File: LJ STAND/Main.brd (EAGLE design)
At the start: 180 x 152 mm, 211 parts, among them Q1 200mA/50V

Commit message: Some small fixes to the main pcb
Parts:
- R15, R24, R33, R42: value 1.5K -> 1K
- moved LOGIC_SWITCH 2.24 mm to (37.1, 56.0)
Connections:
- net LIGHT_GATE_LASER: now also MASTER.21, MASTER.22, MASTER.23
- net LIGHT_GATE_OUT: now also MASTER.20
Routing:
- net LIGHT_GATE_OUT: track 0.00 -> 38.7 mm
- net LIGHT_GATE_LASER: track 0.00 -> 37.1 mm
- net N$12: track 42.9 -> 45.4 mm
- net N$2: track 12.7 -> 15.0 mm
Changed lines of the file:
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@@
 <attribute name="VALUE" x="107.40568125" y="56.8268" size="0.4064" layer="28" font="vector" rot="MR180"/>
 </element>
-<element name="R15" library="SparkFun-Resistors" package="0603-RES" value="1.5K" x="105.4706" y="49.6222" smashed="yes" rot="MR270">
+<element name="R15" library="SparkFun-Resistors" package="0603-RES" value="1K" x="105.4706" y="49.6222" smashed="yes" rot="MR270">
 <attribute name="VALUE" x="104.8606" y="47.86848125" size="0.4064" layer="28" font="vector" rot="MR180"/>
 </element>
@@
 <attribute name="VALUE" x="85.58931875" y="53.3058375" size="0.4064" layer="28" font="vector" rot="MR180"/>
 </element>
-<element name="R24" library="SparkFun-Resistors" package="0603-RES" value="1.5K" x="82.9956" y="54.4308" smashed="yes" rot="MR0">
+<element name="R24" library="SparkFun-Resistors" package="0603-RES" value="1K" x="82.9956" y="54.4308" smashed="yes" rot="MR0">
 <attribute name="VALUE" x="83.595040625" y="53.0744375" size="0.4064" layer="28" font="vector" rot="MR0"/>
 </element>
@@
 <attribute name="VALUE" x="109.9334" y="26.1756" size="0.4064" layer="28" font="vector" rot="MR270"/>
 </element>
-<element name="R33" library="SparkFun-Resistors" package="0603-RES" value="1.5K" x="106.9616" y="23.2394" smashed="yes" rot="MR270">
+<element name="R33" library="SparkFun-Resistors" package="0603-RES" value="1K" x="106.9616" y="23.2394" smashed="yes" rot="MR270">
 <attribute name="VALUE" x="106.239640625" y="21.3788375" size="0.4064" layer="28" font="vector" rot="MR180"/>
 </element>
@@
 <attribute name="VALUE" x="108.42411875" y="41.948278125" size="0.4064" layer="28" font="vector" rot="MR180"/>
 </element>
-<element name="R42" library="SparkFun-Resistors" package="0603-RES" value="1.5K" x="106.3322" y="37.9866" smashed="yes" rot="MR270">
+<element name="R42" library="SparkFun-Resistors" package="0603-RES" value="1K" x="106.3322" y="37.9866" smashed="yes" rot="MR270">
 <attribute name="VALUE" x="105.696121875" y="36.131678125" size="0.4064" layer="28" font="vector" rot="MR180"/>
 </element>
@@
 </element>
 <element name="MOTOR_SWITCH" library="jst-vh" package="B2P-VH" value="" x="39.3702" y="44.6026" smashed="yes" rot="R270">
-<attribute name="NAME" x="44.5546" y="39.3656" size="1.016" layer="25" font="vector" ratio="10" rot="R180"/>
+<attribute name="NAME" x="44.676521875" y="38.5629625" size="1.016" layer="25" font="vector" ratio="10" rot="R180"/>
 <attribute name="VALUE" x="32.3702" y="47.6026" size="1.27" layer="27" rot="R270"/>
 </element>
-<element name="LOGIC_SWITCH" library="jst-vh" package="B2P-VH" value="" x="39.3442" y="56.058" smashed="yes" rot="R270">
-<attribute name="NAME" x="43.945" y="51.0756" size="1.016" layer="25" font="vector" ratio="10" rot="R180"/>
-<attribute name="VALUE" x="32.3442" y="59.058" size="1.27" layer="27" rot="R270"/>
+<element name="LOGIC_SWITCH" library="jst-vh" package="B2P-VH" value="" x="37.109" y="56.0072" smashed="yes" rot="R270">
+<attribute name="NAME" x="41.78091875" y="50.831759375" size="1.016" layer="25" font="vector" ratio="10" rot="R180"/>
+<attribute name="VALUE" x="30.109" y="59.0072" size="1.27" layer="27" rot="R270"/>
 </element>
 <element name="C14" library="SparkFun-Capacitors" package="0805" value="0.1uF" x="42.1638" y="129.4132" smashed="yes" rot="R180">
@@
 <via x="25.3746" y="65.4304" extent="1-16" drill="0.508"/>
 <via x="26.3652" y="52.324" extent="1-16" drill="0.508"/>
-<via x="32.6644" y="57.3786" extent="1-16" drill="0.508"/>
-<via x="32.5882" y="50.3174" extent="1-16" drill="0.508"/>
+<via x="33.528" y="57.195721875" extent="1-16" drill="0.508"/>
+<via x="32.30371875" y="48.265078125" extent="1-16" drill="0.508"/>
 <via x="24.4348" y="44.8056" extent="1-16" drill="0.508"/>
 <via x="29.3116" y="37.7444" extent="1-16" drill="0.508"/>
@@
 <wire x1="60.7074" y1="51.2558" x2="55.245" y2="56.7182" width="5.08" layer="1"/>
 <wire x1="55.245" y1="56.7182" x2="51.954" y2="56.7182" width="5.08" layer="1"/>
-<wire x1="45.466" y1="53.0352" x2="39.5224" y2="53.0352" width="5.08" layer="1"/>
+<wire x1="45.466" y1="53.0352" x2="41.595040625" y2="53.0352" width="5.08" layer="1"/>
+<wire x1="41.595040625" y1="53.0352" x2="39.5224" y2="53.0352" width="5.08" layer="1"/>
 <wire x1="45.466" y1="53.0352" x2="49.1854" y2="56.7546" width="5.08" layer="1"/>
-<wire x1="39.3442" y1="54.078" x2="39.5732" y2="53.849" width="2.54" layer="1"/>
 <wire x1="39.5732" y1="53.086" x2="39.5224" y2="53.0352" width="2.54" layer="1"/>
 <wire x1="39.5732" y1="53.849" x2="39.5732" y2="53.086" width="2.54" layer="1"/>
@@
 <wire x1="51.2318" y1="56.7546" x2="51.2682" y2="56.7182" width="2.54" layer="1"/>
 <wire x1="51.2682" y1="56.7182" x2="51.954" y2="56.7182" width="2.54" layer="1"/>
+<wire x1="37.109" y1="54.0272" x2="38.0502" y2="53.086" width="2.032" layer="1"/>
+<wire x1="38.0502" y1="53.086" x2="39.5732" y2="53.086" width="2.032" layer="1"/>
 </signal>
 <signal name="MOTOR_PWR">
@@
 <contactref element="LOGIC_FUSE" pad="1"/>
 <contactref element="LOGIC_FUSE" pad="2"/>
-<wire x1="39.3442" y1="58.038" x2="43.8656" y2="62.5594" width="2.032" layer="1"/>
-<wire x1="43.8656" y1="62.5594" x2="43.8656" y2="65.5066" width="2.032" layer="1"/>
+<wire x1="43.8656" y1="65.5066" x2="43.8656" y2="62.5594" width="2.032" layer="1"/>
 <wire x1="43.8656" y1="65.5066" x2="43.8656" y2="68.9102" width="2.032" layer="1"/>
-</signal>
-<signal name="N$7">
+<wire x1="43.8656" y1="62.5594" x2="39.2934" y2="57.9872" width="2.032" layer="1"/>
+<wire x1="39.2934" y1="57.9872" x2="37.109" y2="57.9872" width="2.032" layer="1"/>
 </signal>
 <signal name="LED_A_CTRL">
@@
 <signal name="LIGHT_GATE_OUT">
 <contactref element="LIGHT_GATE" pad="2"/>
+<contactref element="MASTER" pad="20"/>
+<wire x1="66.446" y1="119.2018" x2="72.6186" y2="125.3744" width="0.3048" layer="16"/>
+<wire x1="72.6186" y1="125.3744" x2="79.100265625" y2="125.3744" width="0.3048" layer="16"/>
+<wire x1="84.754" y1="111.9811625" x2="85.3751625" y2="111.36" width="0.3048" layer="16"/>
+<wire x1="85.3751625" y1="111.36" x2="90.2536375" y2="111.36" width="0.3048" layer="16"/>
+<wire x1="84.754" y1="119.720665625" x2="84.754" y2="111.9811625" width="0.3048" layer="16"/>
+<wire x1="90.2536375" y1="111.36" x2="91.3140375" y2="112.4204" width="0.3048" layer="16"/>
+<wire x1="91.3140375" y1="112.4204" x2="91.8144" y2="112.4204" width="0.3048" layer="16"/>
+<wire x1="79.100265625" y1="125.3744" x2="84.754" y2="119.720665625" width="0.3048" layer="16"/>
 </signal>
 <signal name="LIGHT_GATE_LASER">
 <contactref element="LIGHT_GATE" pad="3"/>
+<contactref element="MASTER" pad="23"/>
+<contactref element="MASTER" pad="21"/>
+<contactref element="MASTER" pad="22"/>
+<wire x1="89.8144" y1="112.4204" x2="89.59088125" y2="112.64391875" width="0.3048" layer="16"/>
+<wire x1="89.59088125" y1="112.64391875" x2="89.59088125" y2="115.60220625" width="0.3048" layer="16"/>
+<wire x1="73.34766875" y1="127.9144" x2="73.32735" y2="127.89408125" width="0.3048" layer="16"/>
+<wire x1="89.59088125" y1="115.60220625" x2="77.2786875" y2="127.9144" width="0.3048" layer="16"/>
+<wire x1="77.2786875" y1="127.9144" x2="73.34766875" y2="127.9144" width="0.3048" layer="16"/>
+<wire x1="67.51828125" y1="127.89408125" x2="66.446" y2="126.8218" width="0.3048" layer="16"/>
+<wire x1="73.32735" y1="127.89408125" x2="67.51828125" y2="127.89408125" width="0.3048" layer="16"/>
+<wire x1="66.446" y1="126.8218" x2="66.446" y2="124.2818" width="0.3048" layer="16"/>
+<wire x1="66.446" y1="124.2818" x2="66.446" y2="121.7418" width="0.3048" layer="16"/>
 </signal>
 <signal name="N$61">

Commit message: Light gate plug labels
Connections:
- removed net N$61: LIGHT_GATE.4
- net GND: now also LIGHT_GATE.4
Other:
- board text added: "LASER"
- board text added: "OUT"
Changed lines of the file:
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@@
 </layers>
 <board>
-<fusionsync huburn="a.cGVyc29uYWw6dWUyYTBjMzI3" projecturn="a.cGVyc29uYWw6dWUyYTBjMzI3IzIwMTgwMjIxMTE4OTc1ODMx" f3durn="urn:adsk.wipprod:dm.lineage:UXq9haHARHGsp8KBzdPV8g" pcbguid="e727809a-a4e0-4e04-8e07-69960e436c38" lastpulledtime="2018-03-07T08:26:08Z" lastsyncedchangeguid="06bce655-d89b-cb29-9812-97d923b35caf"/>
+<fusionsync huburn="a.cGVyc29uYWw6dWUyYTBjMzI3" projecturn="a.cGVyc29uYWw6dWUyYTBjMzI3IzIwMTgwMjIxMTE4OTc1ODMx" f3durn="urn:adsk.wipprod:dm.lineage:UXq9haHARHGsp8KBzdPV8g" pcbguid="e727809a-a4e0-4e04-8e07-69960e436c38" lastpulledtime="2018-03-07T08:26:08Z" lastsyncedchangeguid="1b572490-dd75-8db9-c1bc-0cb30423e8fc"/>
 <plain>
 <wire x1="147.5601" y1="138.2534" x2="151.5573" y2="136.257" width="0.254" layer="52" curve="-53.077158" locked="yes"/>
@@
 <text x="90.79991875" y="92.16135625" size="1.016" layer="22" font="vector" ratio="15" rot="MR90">CS2</text>
 <text x="93.380559375" y="92.202" size="1.016" layer="22" font="vector" ratio="15" rot="MR90">CS3</text>
+<text x="85.2424" y="115.38711875" size="1.016" layer="22" font="vector" ratio="15" rot="MR90">GND</text>
+<text x="87.25408125" y="115.315996875" size="1.016" layer="22" font="vector" ratio="15" rot="MR90">GND</text>
+<text x="89.33688125" y="115.295675" size="1.016" layer="22" font="vector" ratio="15" rot="MR90">LASER</text>
+<text x="91.399359375" y="115.285515625" size="1.016" layer="22" font="vector" ratio="15" rot="MR90">OUT</text>
+<text x="93.4212" y="115.285515625" size="1.016" layer="22" font="vector" ratio="15" rot="MR90">3.3V</text>
+<text x="85.2424" y="115.315996875" size="1.016" layer="22" font="vector" ratio="15" rot="MR90">GND</text>
 </plain>
 <attributes>
@@
 <element name="U$2" library="Gyro" package="GYRO" value="GYRO" x="89.9922" y="98.1202" smashed="yes" rot="MR180"/>
 <element name="LIGHT_GATE" library="jst-ph" library_urn="urn:adsk.eagle:library:1951258" package="B5B-PH-K-S" package3d_urn="urn:adsk.eagle:package:1951342/1" value="" x="89.8144" y="112.4204" smashed="yes" rot="MR0">
-<attribute name="NAME" x="94.9" y="115.621440625" size="1.27" layer="26" font="vector" ratio="10" rot="MR0"/>
+<attribute name="NAME" x="81.839440625" y="106.989359375" size="1.27" layer="26" font="vector" ratio="10" rot="MR90"/>
 <attribute name="VALUE" x="95.8144" y="107.9204" size="1.27" layer="28" rot="MR0"/>
 </element>
@@
 <via x="148.117559375" y="47.9298" extent="1-16" drill="0.508"/>
 <via x="154.6098" y="60.2488" extent="1-16" drill="0.508"/>
+<contactref element="LIGHT_GATE" pad="4"/>
 </signal>
 <signal name="N$12">
@@
 <wire x1="66.446" y1="124.2818" x2="66.446" y2="121.7418" width="0.3048" layer="16"/>
 </signal>
-<signal name="N$61">
-<contactref element="LIGHT_GATE" pad="4"/>
-</signal>
 <signal name="N$58">

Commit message: Main edits, light gate pcbs
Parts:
- added C18, C19: 0.1uF, SparkFun-Capacitors:0805
- BT_DEBUG_LED, BT_IRC_LED: value (none) -> BLUE
- moved LIGHT_GATE 3.96 mm to (89.7, 116.4)
- moved C66 1.54 mm to (96.1, 146.1)
- moved C73 0.78 mm to (15.0, 52.9)
- moved C62 0.51 mm to (20.3, 136.5)
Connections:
- net 3.3V: now also C18.1, C19.1
- net GND: now also C18.2, C19.2
- net N$11: now also D1.NOP
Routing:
- net 3.3V: track 851.4 -> 830.3 mm, vias 29 -> 32
- net 5V: track 677.3 -> 671.6 mm
- net N$11: track 19.3 -> 24.3 mm
- net LIGHT_GATE_OUT: track 38.7 -> 34.7 mm
- net LIGHT_GATE_LASER: track 37.1 -> 33.6 mm
- net GND: track 251.8 -> 254.8 mm
- net IR_PWR: track 617.0 -> 615.7 mm
- net N$51: track 565.8 -> 566.8 mm
- net N$70: track 46.3 -> 47.0 mm

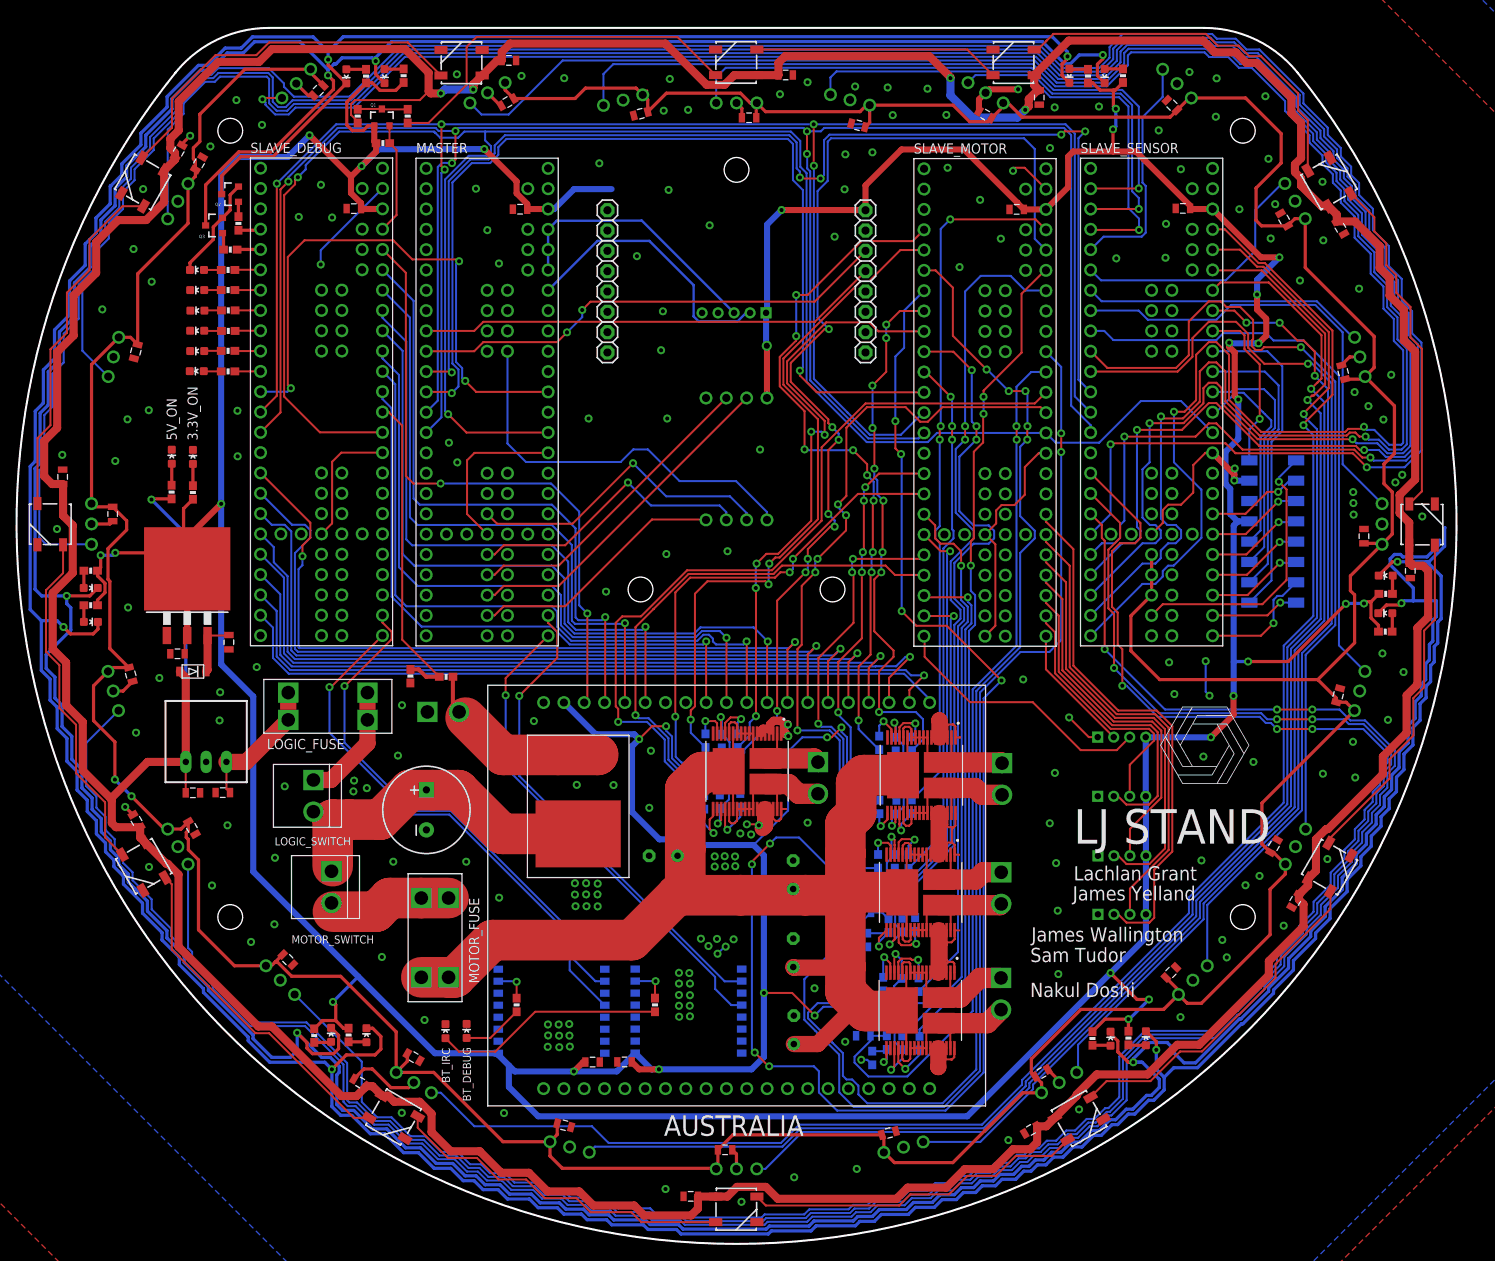
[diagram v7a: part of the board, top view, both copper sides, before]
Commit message: Finalisation of gyro, encoder and light boards + gerbers, silkscreen fixes
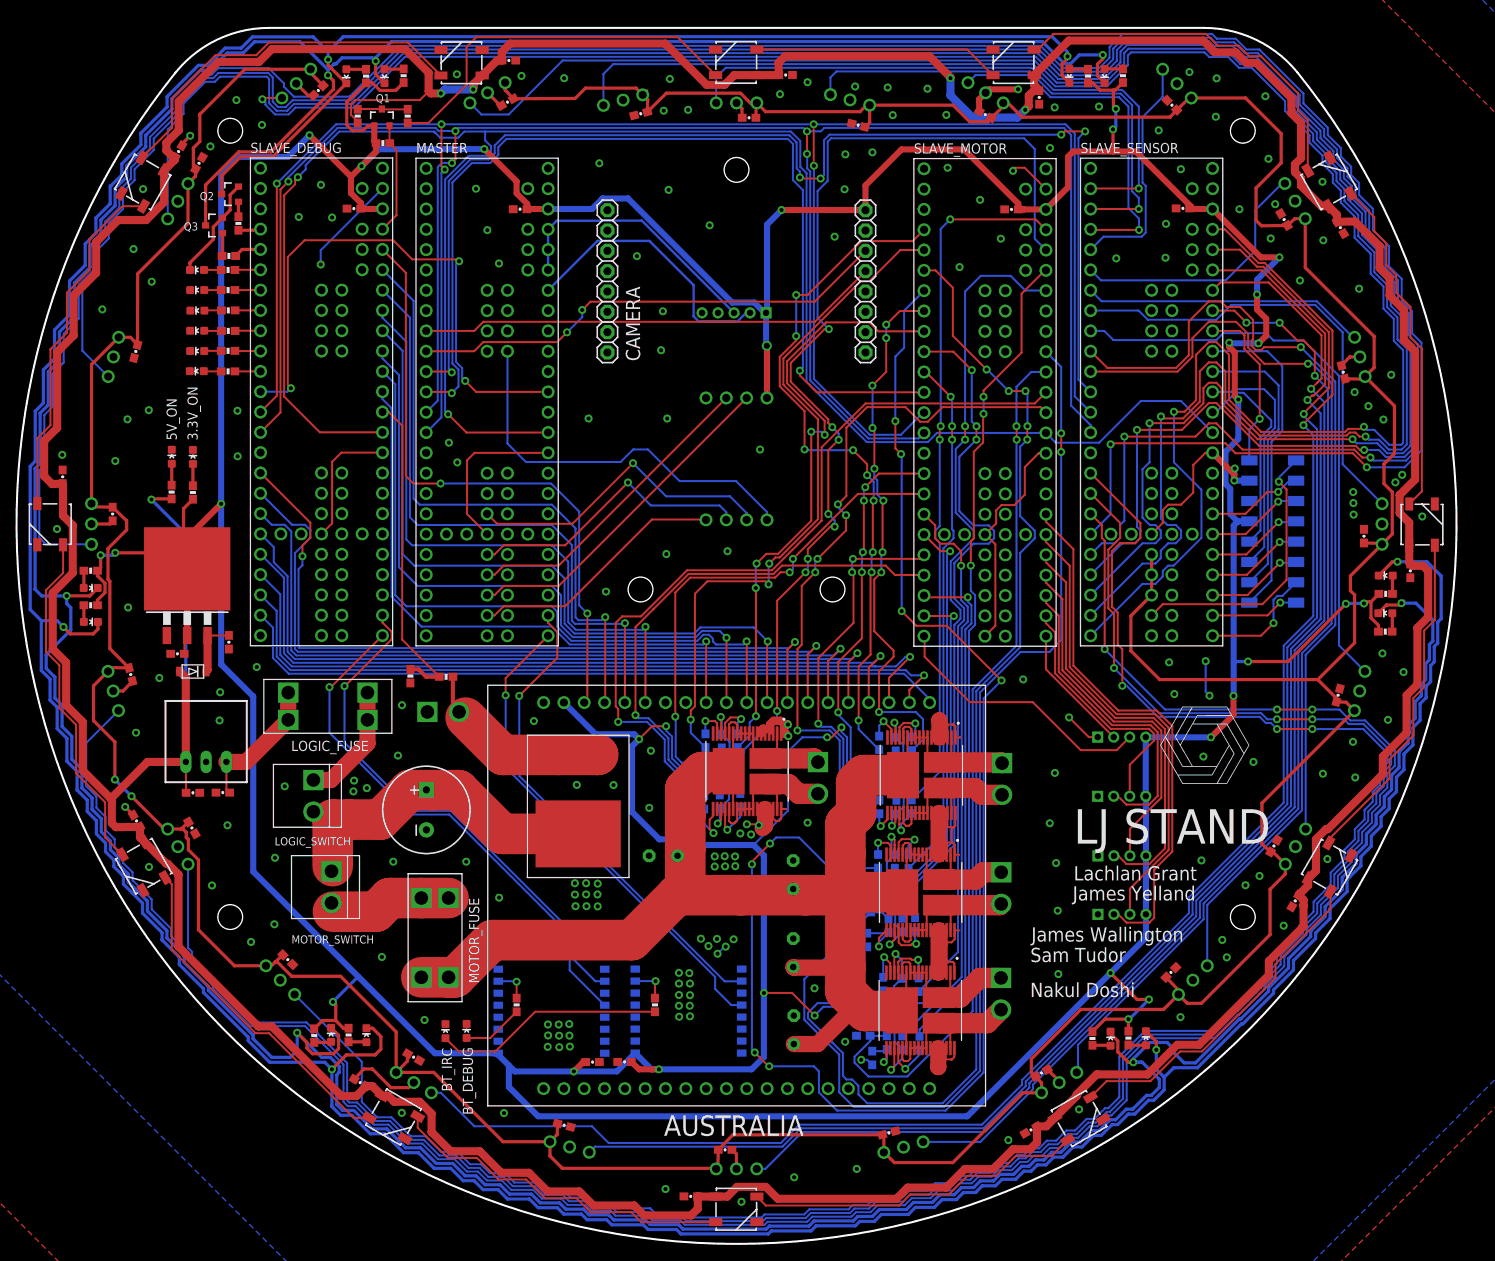
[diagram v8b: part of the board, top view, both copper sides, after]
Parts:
- C11, C12, C13, C14, C15, C16, C17, C18, C19, C2, C3, C38, C39, C4, C40, C41, C42, C43, C44, C45, C46, C47, C48, C49, C5, C50, C51, C52, C53, C54, C55, C56, C57, C58, C59, C6, C60, C61, C62, C63, C64, C65, C66, C67, C68, C69, C70, C71, C72, C73: device SparkFun-Capacitors:0805 -> SparkFun-Capacitors:0603-CAP
- moved R62 0.80 mm to (26.5, 123.5)
- moved C17 0.65 mm to (124.4, 129.3)
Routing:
- net 3.3V: track 830.3 -> 855.7 mm
- net N$51: track 566.8 -> 550.8 mm
- net N$10: track 542.8 -> 537.4 mm
- net 5V: track 671.6 -> 672.5 mm
- net N$59: track 2.13 -> 3.06 mm
- net IR_PWR: track 615.7 -> 615.1 mm
- net LED_D_CTRL: track 2.94 -> 3.45 mm
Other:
- board text added: "1"
- board text added: "CAMERA"
- board text added: "fire water earth air hardware software"
